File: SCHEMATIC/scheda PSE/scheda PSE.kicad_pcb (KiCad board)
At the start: 2 copper layers, 102.4 x 77.4 mm, 148 parts, among them J1 Conn_01x03, J2 Vin, J3 USB_B_Mini, J4 Vout 5V, J5 I2C_3V3, J6 UART0_3V3, Q1 IRLML0060TRPBF, Q2 PDTC114YT, Q3 IRLML9301, SW1 RESET_SW, SW2 PROG_SW, SW3 SW_U, SW4 SW_L, SW5 SW_R, SW6 SW_D, SW7 Power_button, U1 RP2040, U2 W25Q16JVUSSQ, U3 AT24C256, U4 oled_0.96"_128x64px, U5 TPS563201, U6 XC6705A331MR-G, U7 SAM-M8Q, U8 MMA8451Q, U9 TC1047A, Y1 12MHz

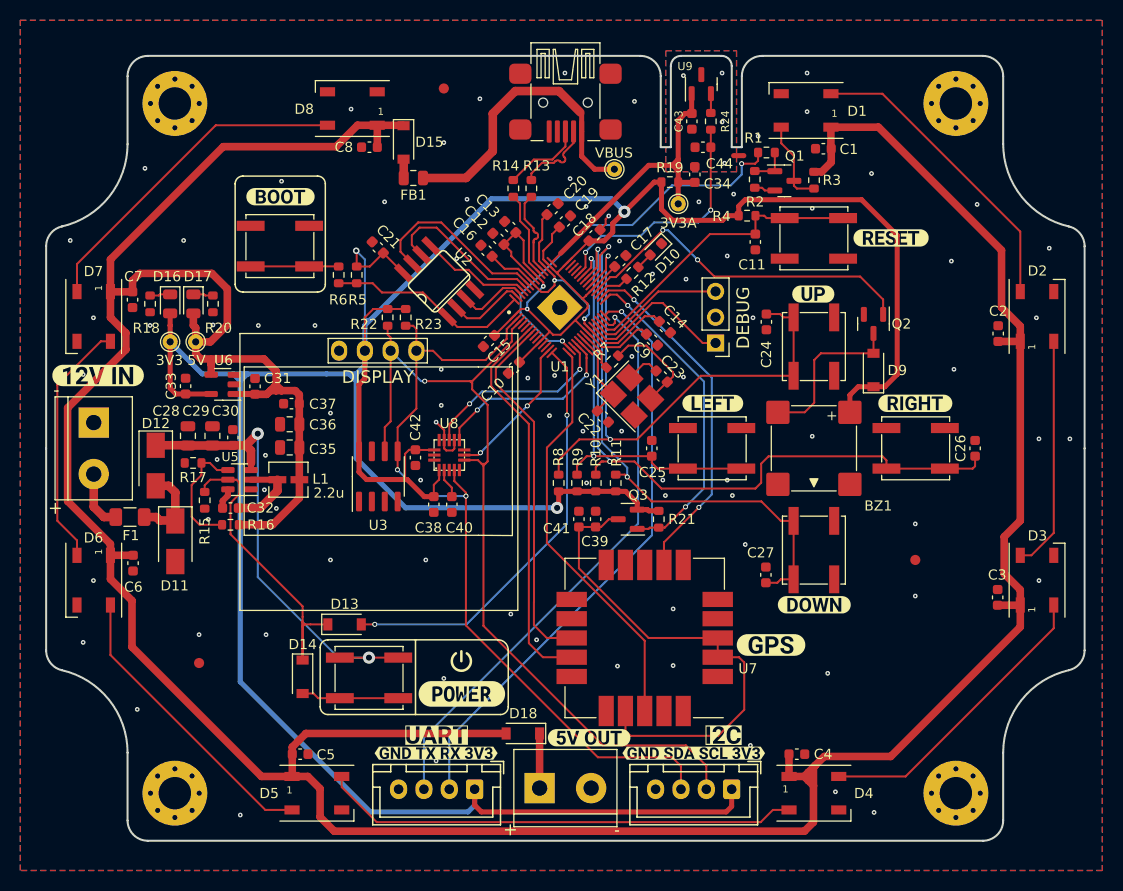
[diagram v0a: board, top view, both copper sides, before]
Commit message: Aggiunte tutte le cose richieste dal prof
Aggiunte tutte le cose richieste dal prof:
wifi
servo
uscita led
MANCA DA METERE IL SOLDER MASK SUI PAD NON USATI DEL GPS
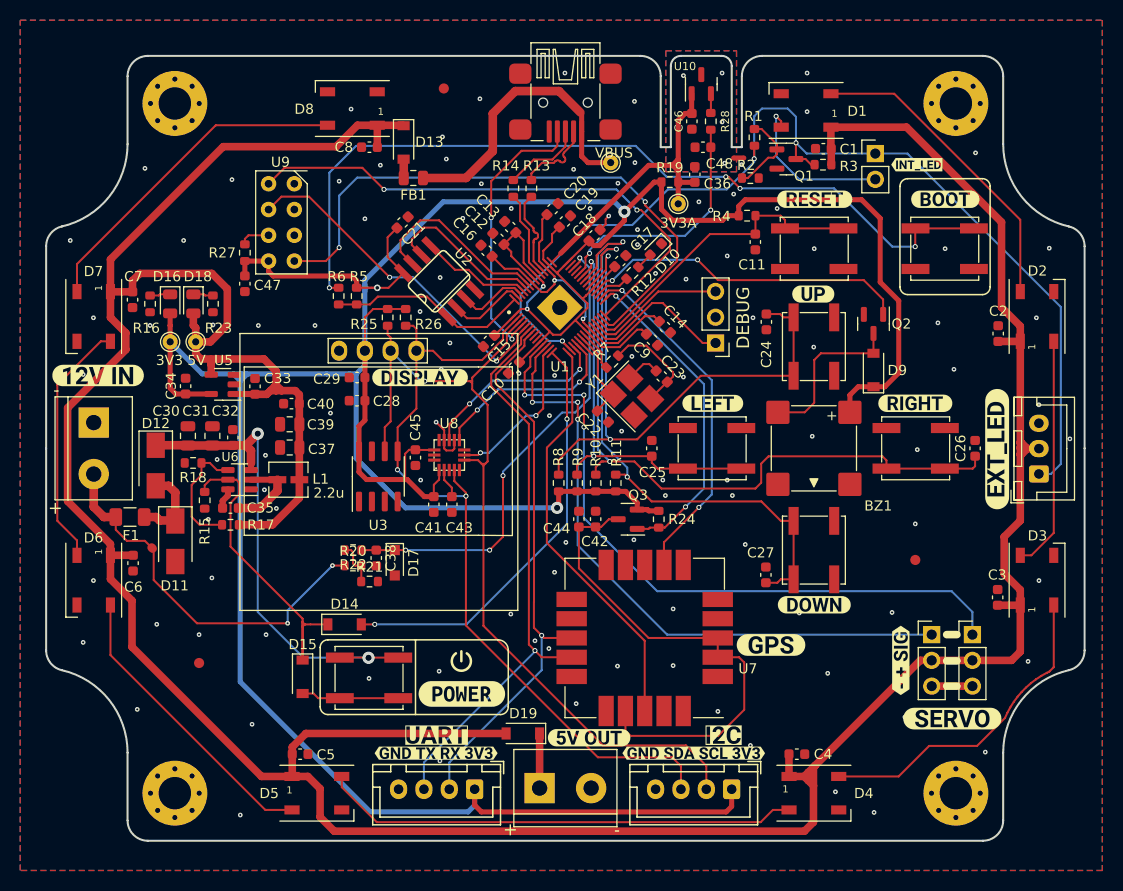
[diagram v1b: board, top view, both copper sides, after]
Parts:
- added C28: 4.7u, Capacitor_SMD:C_0603_1608Metric, F.Cu at (135.0, 92.3)
- added C29: 100n, Capacitor_SMD:C_0603_1608Metric, F.Cu at (135.0, 90.0)
- added C38: 100n, Capacitor_SMD:C_0603_1608Metric, F.Cu at (136.9, 107.8)
- added C47: 100n, Capacitor_SMD:C_0603_1608Metric, F.Cu at (123.9, 80.8)
- added D17: PDZ3.3B.115, Diode_SMD:D_SOD-323_HandSoldering, F.Cu at (138.7, 108.3)
- added J1: WS2812B, Connector_JST:JST_XH_B3B-XH-A_1x03_P2.50mm_Vertical, F.Cu at (202.2, 99.5)
- added J8: SERVO_1, Connector_PinHeader_2.54mm:PinHeader_1x03_P2.54mm_Vertical, F.Cu at (195.6, 115.4)
- added J9: SERVO_2, Connector_PinHeader_2.54mm:PinHeader_1x03_P2.54mm_Vertical, F.Cu at (191.6, 115.4)
- added JP1: EXT_LEDs, Connector_PinHeader_2.54mm:PinHeader_1x02_P2.54mm_Vertical, F.Cu at (186.1, 67.9)
- added R20: 150k, Resistor_SMD:R_0603_1608Metric, F.Cu at (134.6, 108.6)
- added R21: 56k, Resistor_SMD:R_0603_1608Metric, F.Cu at (136.2, 110.1)
- added R22: 1k, Resistor_SMD:R_0603_1608Metric, F.Cu at (134.6, 107.0)
- added R27: 10K, Resistor_SMD:R_0603_1608Metric, F.Cu at (123.9, 77.7)
- added U9: ESP-01, _PSE:ESP-01, F.Cu at (128.8, 74.7)
- added kibuzzard-643D3A9E: G***, kibuzzard-643D3A9E, F.Cu at (141.2, 90.0)
- added kibuzzard-643DAACA: G***, kibuzzard-643DAACA, F.Cu at (193.6, 123.6)
- added kibuzzard-643DAE7D: G***, kibuzzard-643DAE7D, F.Cu at (198.1, 97.1)
- added kibuzzard-643DB02D: G***, kibuzzard-643DB02D, F.Cu at (188.6, 117.9)
- added kibuzzard-643DB063: G***, kibuzzard-643DB063, B.Cu at (188.6, 117.9)
- added kibuzzard-643DB07D: G***, kibuzzard-643DB07D, B.Cu at (199.4, 97.1)
- added kibuzzard-643DB1BA: G***, kibuzzard-643DB1BA, F.Cu at (190.1, 69.0)
- R3: value 10k -> 1k
- moved SW2 65.5 mm to (192.9, 77.3), turned to 0 degrees
- moved kibuzzard-643CF9C9 65.5 mm to (193.0, 72.4)
- moved kibuzzard-643CF9B2 8.44 mm to (180.1, 72.4)
- moved C21 3.47 mm to (139.4, 74.7), turned to 45 degrees
- moved Q1 2.16 mm to (177.3, 68.5)
- moved R5 2.09 mm to (134.9, 82.0)
- moved R6 2.09 mm to (133.1, 82.0)
- moved R1 1.90 mm to (174.1, 66.3), turned to 90 degrees
- moved R3 1.77 mm to (180.9, 69.0), turned to 0 degrees
- moved SW1 1.02 mm to (180.0, 77.3)
- moved TP1 0.74 mm to (160.0, 68.8)
- moved R2 0.45 mm to (173.7, 70.4), turned to 180 degrees
- moved NT1 0.23 mm to (172.6, 68.4)
- renumbered C28 to C30, C29 to C31, C30 to C32, C31 to C33, C33 to C34, C32 to C35, C34 to C36, C35 to C37, C36 to C39, C37 to C40, C38 to C41, C39 to C42, C40 to C43, C41 to C44, C42 to C45, C43 to C46, C44 to C48, D15 to D13, D13 to D14, D14 to D15, D17 to D18, D18 to D19, J1 to J2, J2 to J3, J3 to J4, J4 to J5, J5 to J6, J6 to J7, R18 to R16, R16 to R17, R17 to R18, R20 to R23, R21 to R24, R22 to R25, R23 to R26, R24 to R28, U9 to U10, U6 to U5, U5 to U6
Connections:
- J4 pad 4: unconnected-(J3-Pad4) -> /Alimentazione/USB _ID
- J7 pad 2: /UART0_RX -> /Sensori/UART_TX
- J7 pad 3: /UART0_TX -> /Sensori/UART_RX
- Q1 pad 3: Net-(D1-Pad4) -> /Led_RGB_WS2812B/DIN
- R3 pad 1: Net-(D1-Pad4) -> /Led_RGB_WS2812B/DIN
- U1 pad 11: unconnected-(U1-Pad11) -> /RP2040/PWM_SERVO1
- U1 pad 12: unconnected-(U1-Pad12) -> /RP2040/PWM_SERVO2
- U1 pad 27: /UART0_TX -> /RP2040/UART0_TX
- U1 pad 28: /UART0_RX -> /RP2040/UART0_RX
- U1 pad 4: unconnected-(U1-Pad4) -> /Alimentazione/USB _ID
- U1 pad 40: unconnected-(U1-Pad40) -> /Alimentazione/ANALOG_BATT
- U1 pad 5: unconnected-(U1-Pad5) -> /RP2040/ESP-01_EN
- U1 pad 6: /UART_TX -> /Sensori/UART_RX
- U1 pad 7: /UART_RX -> /Sensori/UART_TX
- U7 pad 13: /UART_RX -> /Sensori/UART_TX
- U7 pad 14: /UART_TX -> /Sensori/UART_RX
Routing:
- net /RP2040/~{USB_BOOT}: track 8.68 -> 82.8 mm, vias 0 -> 4
- net /RP2040/PWM_SERVO1: track 0.00 -> 68.1 mm, vias 0 -> 3
- net /Led_RGB_WS2812B/DIN: track 38.6 -> 104.4 mm, vias 2 -> 3
- net /RP2040/PWM_SERVO2: track 0.00 -> 63.1 mm, vias 0 -> 3
- net /RP2040/UART0_TX: track 0.00 -> 59.4 mm, vias 0 -> 2
- net /UART0_RX: track 58.4 -> 0.00 mm, vias 1 -> 0
- net /UART0_TX: track 58.4 -> 0.00 mm, vias 1 -> 0
- net /Sensori/UART_RX: track 0.00 -> 57.0 mm, vias 0 -> 1
- net /Sensori/UART_TX: track 0.00 -> 55.2 mm, vias 0 -> 1
- net /RP2040/UART0_RX: track 0.00 -> 53.3 mm, vias 0 -> 2
- net /Alimentazione/ANALOG_BATT: track 0.00 -> 47.9 mm, vias 0 -> 4
- net /UART_TX: track 38.8 -> 0.00 mm
- net /UART_RX: track 36.1 -> 0.00 mm
- net /RP2040/ESP-01_EN: track 0.00 -> 34.3 mm, vias 0 -> 2
- net /Alimentazione/VIN: track 5.82 -> 38.3 mm, vias 0 -> 2
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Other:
- board text removed: "DISPLAY"

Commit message: Sistemate un po'di cose
aggiuno fori display e terzo servo e sistemate le serigrafie
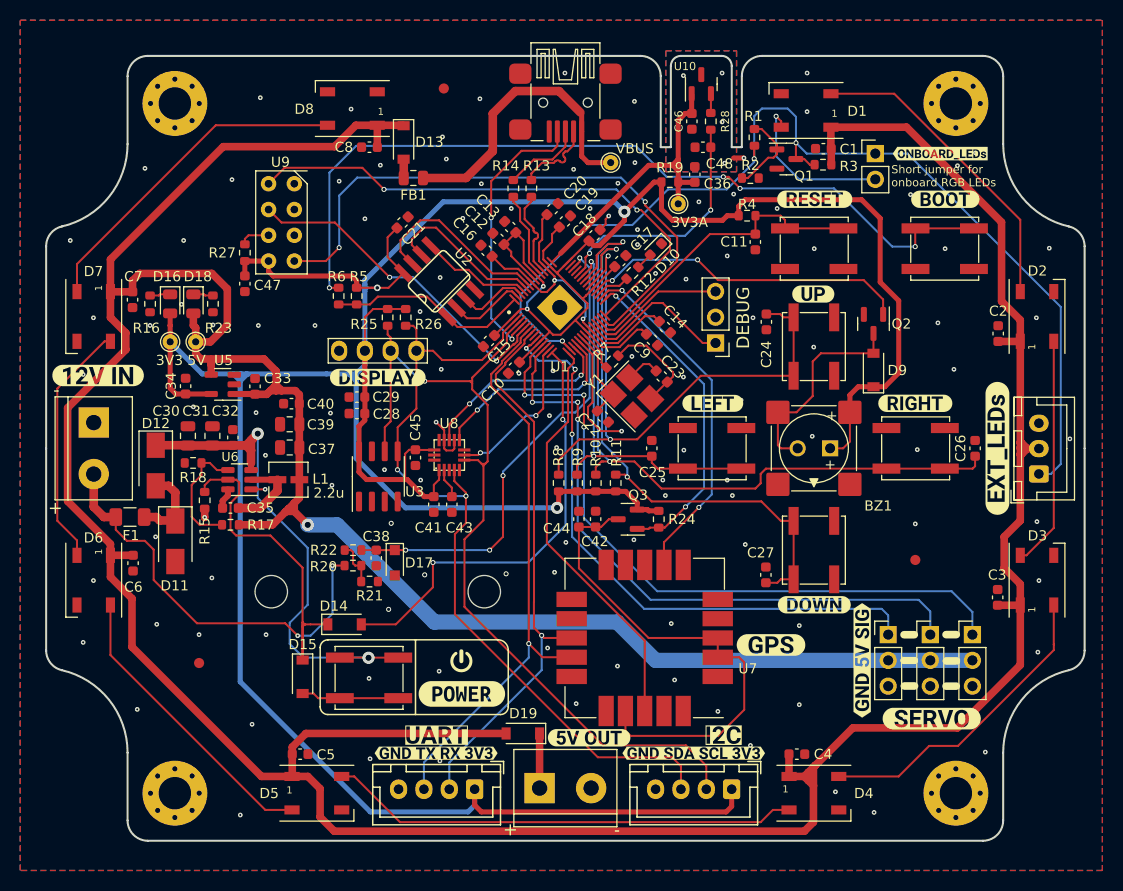
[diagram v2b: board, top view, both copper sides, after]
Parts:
- removed kibuzzard-643DAE7D: G***, kibuzzard-643DAE7D
- removed kibuzzard-643DB02D: G***, kibuzzard-643DB02D
- removed kibuzzard-643DB063: G***, kibuzzard-643DB063
- removed kibuzzard-643DB07D: G***, kibuzzard-643DB07D
- removed kibuzzard-643DB1BA: G***, kibuzzard-643DB1BA
- added J10: SERVO_3, Connector_PinHeader_2.54mm:PinHeader_1x03_P2.54mm_Vertical, F.Cu at (187.3, 115.4)
- added REF**: MountingHole_3.2mm_M3, MountingHole:MountingHole_3.2mm_M3, F.Cu at (147.5, 111.1)
- added REF**: MagneticBuzzer_Kingstate_KCG0601, Buzzer_Beeper:MagneticBuzzer_Kingstate_KCG0601, F.Cu at (181.6, 97.0)
- added REF**: MountingHole_3.2mm_M3, MountingHole:MountingHole_3.2mm_M3, F.Cu at (126.5, 111.1)
- added kibuzzard-643E45B9: G***, kibuzzard-643E45B9, B.Cu at (198.5, 97.0)
- added kibuzzard-643E45C8: G***, kibuzzard-643E45C8, B.Cu at (184.7, 117.9)
- added kibuzzard-643E45D3: G***, kibuzzard-643E45D3, F.Cu at (184.8, 117.9)
- added kibuzzard-643E4714: G***, kibuzzard-643E4714, F.Cu at (192.5, 67.9)
- added kibuzzard-643E4784: G***, kibuzzard-643E4784, F.Cu at (198.1, 97.0)
- moved U4 10.6 mm to (137.0, 87.4)
- moved kibuzzard-643D3A9E 4.17 mm to (137.0, 90.0)
- moved kibuzzard-643DAACA 2.03 mm to (191.6, 123.6)
- moved C29 1.93 mm to (135.0, 91.9)
- moved C28 1.27 mm to (135.0, 93.6)
- moved J9 0.14 mm to (191.5, 115.4)
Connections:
- U1 pad 9: unconnected-(U1-Pad9) -> /RP2040/PWM_SERVO3
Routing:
- net +5V: track 361.5 -> 437.7 mm, vias 0 -> 1
- net /RP2040/PWM_SERVO3: track 0.00 -> 60.1 mm, vias 0 -> 3
- net GND: track 16.0 -> 24.5 mm, vias 108 -> 120
- net +3V3: track 391.2 -> 396.3 mm
- net Net-(BZ1-Pad2): track 16.3 -> 21.1 mm
- net /Alimentazione/VIN: track 38.3 -> 41.4 mm
- net +12V: track 49.3 -> 52.1 mm
- net /Interfaccia utente/BUTTON_R: track 73.9 -> 71.8 mm
- net /Alimentazione/BUCK_EN: track 32.1 -> 33.9 mm
- net /I2C0_SCL: track 87.6 -> 89.1 mm
- net /Alimentazione/5V_EN: track 41.9 -> 43.2 mm
- net Net-(D3-Pad2): track 32.0 -> 30.8 mm
- net /RP2040/ESP-01_EN: track 34.3 -> 33.3 mm
- net /I2C0_SDA: track 81.3 -> 82.2 mm
- net /RP2040/INT1_ACC: track 19.1 -> 19.8 mm
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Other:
- board text added: "Short jumper for onboard RGB LEDs"

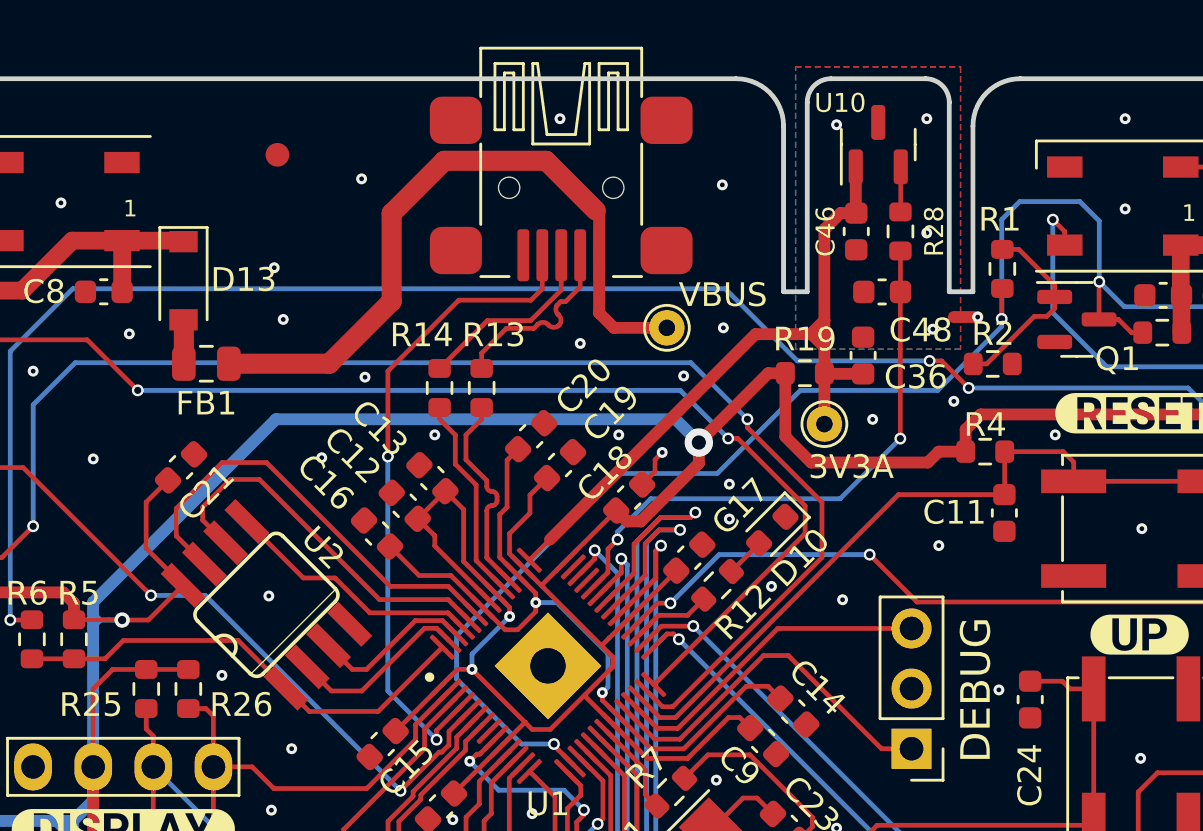
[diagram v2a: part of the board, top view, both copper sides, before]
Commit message: Aggiunto mosfet uscita corrente usb
Ultima modifica prima della revisone generale.
aggiunto un mosfet P per l'attivazione dell'uscita della tensione alla usb in caso di master
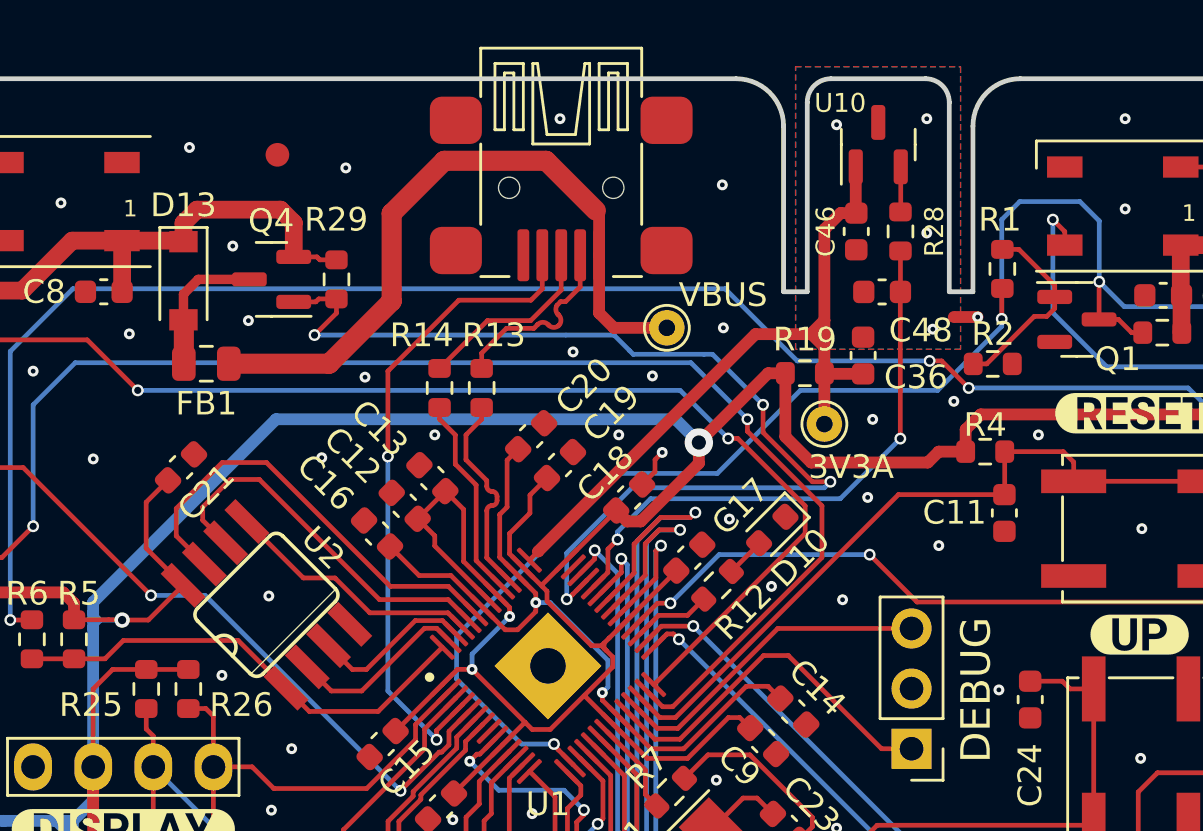
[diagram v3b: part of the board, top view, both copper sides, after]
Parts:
- added Q4: IRLML9301, Package_TO_SOT_SMD:SOT-23, F.Cu at (143.3, 66.8)
- added R29: 10k, Resistor_SMD:R_0603_1608Metric, F.Cu at (146.0, 66.8)
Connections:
- U1 pad 39: unconnected-(U1-Pad39) -> /Alimentazione/OUTPUT_USB_EN
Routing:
- net /Alimentazione/OUTPUT_USB_EN: track 0.00 -> 44.3 mm, vias 0 -> 4
- net +5V: track 437.7 -> 446.9 mm
- net /Alimentazione/FILTERED_VBUS: track 1.86 -> 5.99 mm
- net +3V3: track 396.3 -> 396.9 mm
- net GND: vias 120 -> 121

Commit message: Versione definitiva inviata ai prof
Sistemato tutto e inviato il tutto ai prof
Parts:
- removed kibuzzard-643E45B9: G***, kibuzzard-643E45B9
- added R30: 47k, Resistor_SMD:R_0603_1608Metric, F.Cu at (145.1, 72.1)
- added kibuzzard-644128D0: G***, kibuzzard-644128D0, B.Cu at (198.5, 97.0)
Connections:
- J1 pad 1: /Led_RGB_WS2812B/DIN -> /Led_RGB_WS2812B/DIN_INT
- J7 pad 2: /Sensori/UART_TX -> /Sensori/UART_RX
- J7 pad 3: /Sensori/UART_RX -> /Sensori/UART_TX
- JP1 pad 1: /Led_RGB_WS2812B/DIN -> /Led_RGB_WS2812B/DIN_INT
- Q1 pad 3: /Led_RGB_WS2812B/DIN -> /Led_RGB_WS2812B/DIN_INT
- R3 pad 1: /Led_RGB_WS2812B/DIN -> /Led_RGB_WS2812B/DIN_INT
- U1 pad 13: /RP2040/ACC_SA0 -> unconnected-(U1-Pad13)
- U1 pad 6: /Sensori/UART_RX -> /Sensori/UART_TX
- U1 pad 7: /Sensori/UART_TX -> /Sensori/UART_RX
- U7 pad 13: /Sensori/UART_TX -> /Sensori/UART_RX
- U7 pad 14: /Sensori/UART_RX -> /Sensori/UART_TX
- U8 pad 7: /RP2040/ACC_SA0 -> GND
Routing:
- net /Led_RGB_WS2812B/DIN: track 104.4 -> 39.8 mm, vias 3 -> 2
- net /Led_RGB_WS2812B/DIN_INT: track 0.00 -> 54.5 mm, vias 0 -> 1
- net /RP2040/ACC_SA0: track 15.7 -> 0.00 mm, vias 2 -> 0
- net /Alimentazione/USB _ID: track 27.7 -> 30.4 mm
- net /Sensori/UART_TX: track 55.2 -> 57.4 mm
- net /Sensori/UART_RX: track 57.4 -> 55.2 mm
- net GND: track 24.5 -> 26.2 mm, vias 121 -> 125
- net /RP2040/UART0_RX: track 53.3 -> 54.3 mm
- net /Alimentazione/ANALOG_BATT: track 47.9 -> 48.7 mm
- net /Alimentazione/5V_EN: track 43.2 -> 43.7 mm
